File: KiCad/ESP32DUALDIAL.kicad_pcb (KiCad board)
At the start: 2 copper layers, 200 x 70 mm, 39 parts, among them J1 SERVICE, J2 100V IN, J3 FAN, J4 FAN, J5 POWER CONTROL, Q1 Q_NMOS_GDS, SW1 Rotary_Encoder_Switch, SW2 Rotary_Encoder_Switch, U1 CR2013-MI2120, U2 ESP-WROOM-32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

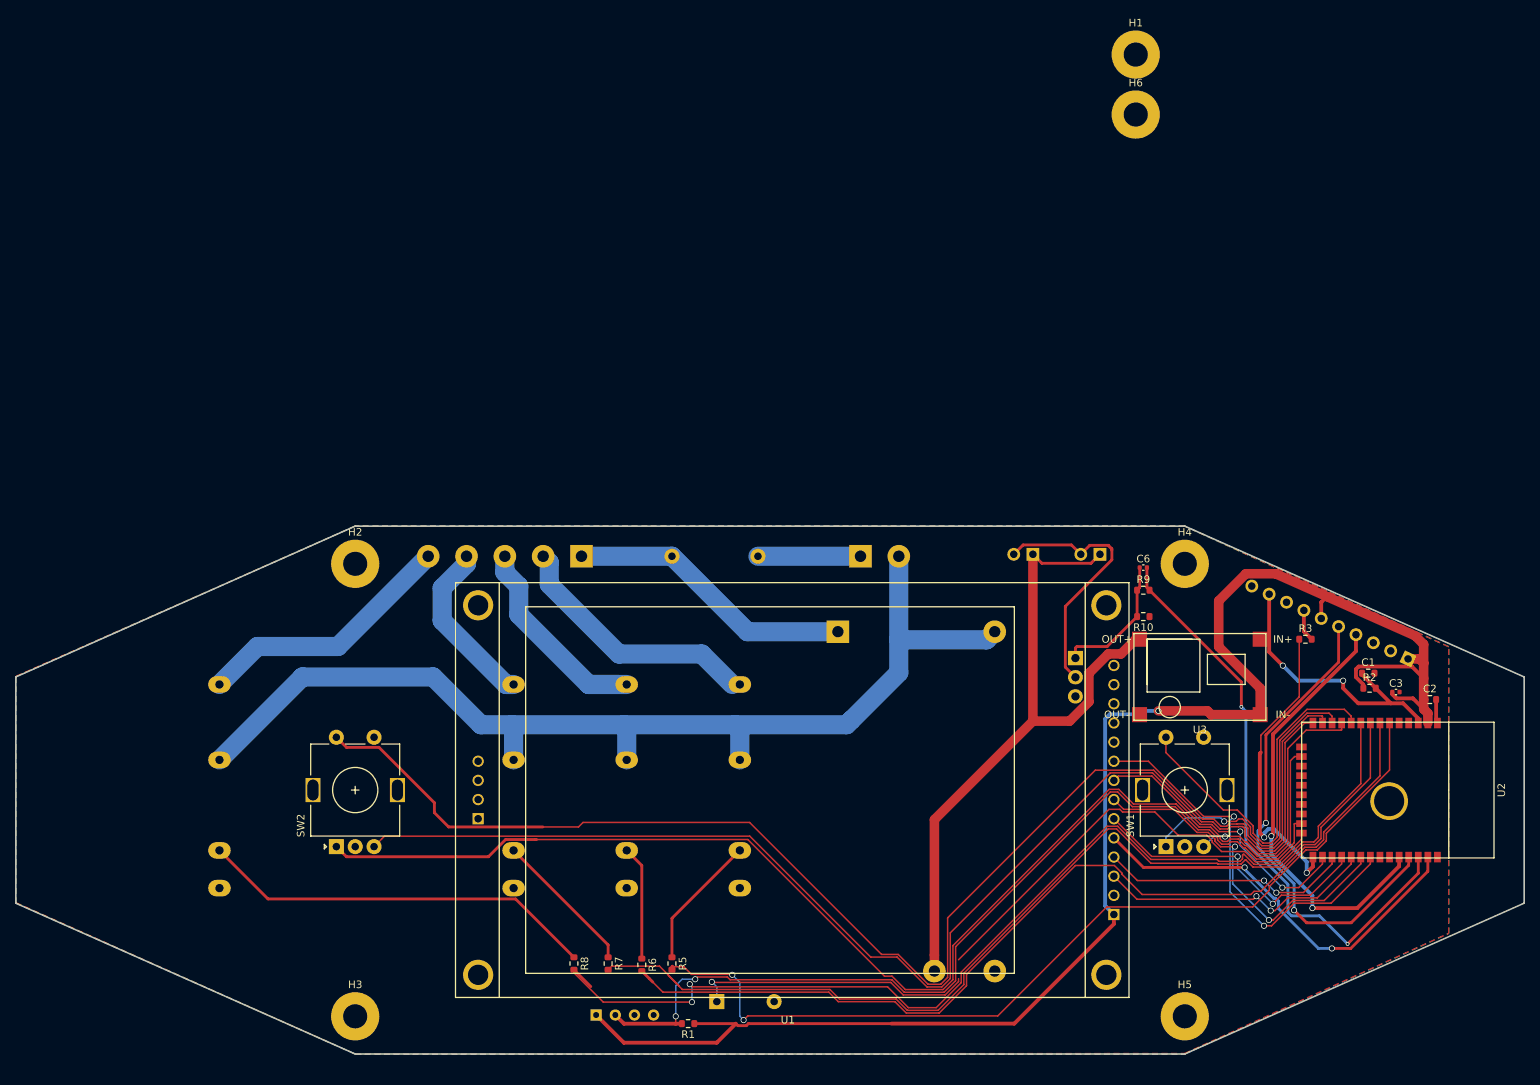
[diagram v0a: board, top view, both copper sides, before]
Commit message: change SSR SHARP S108T02
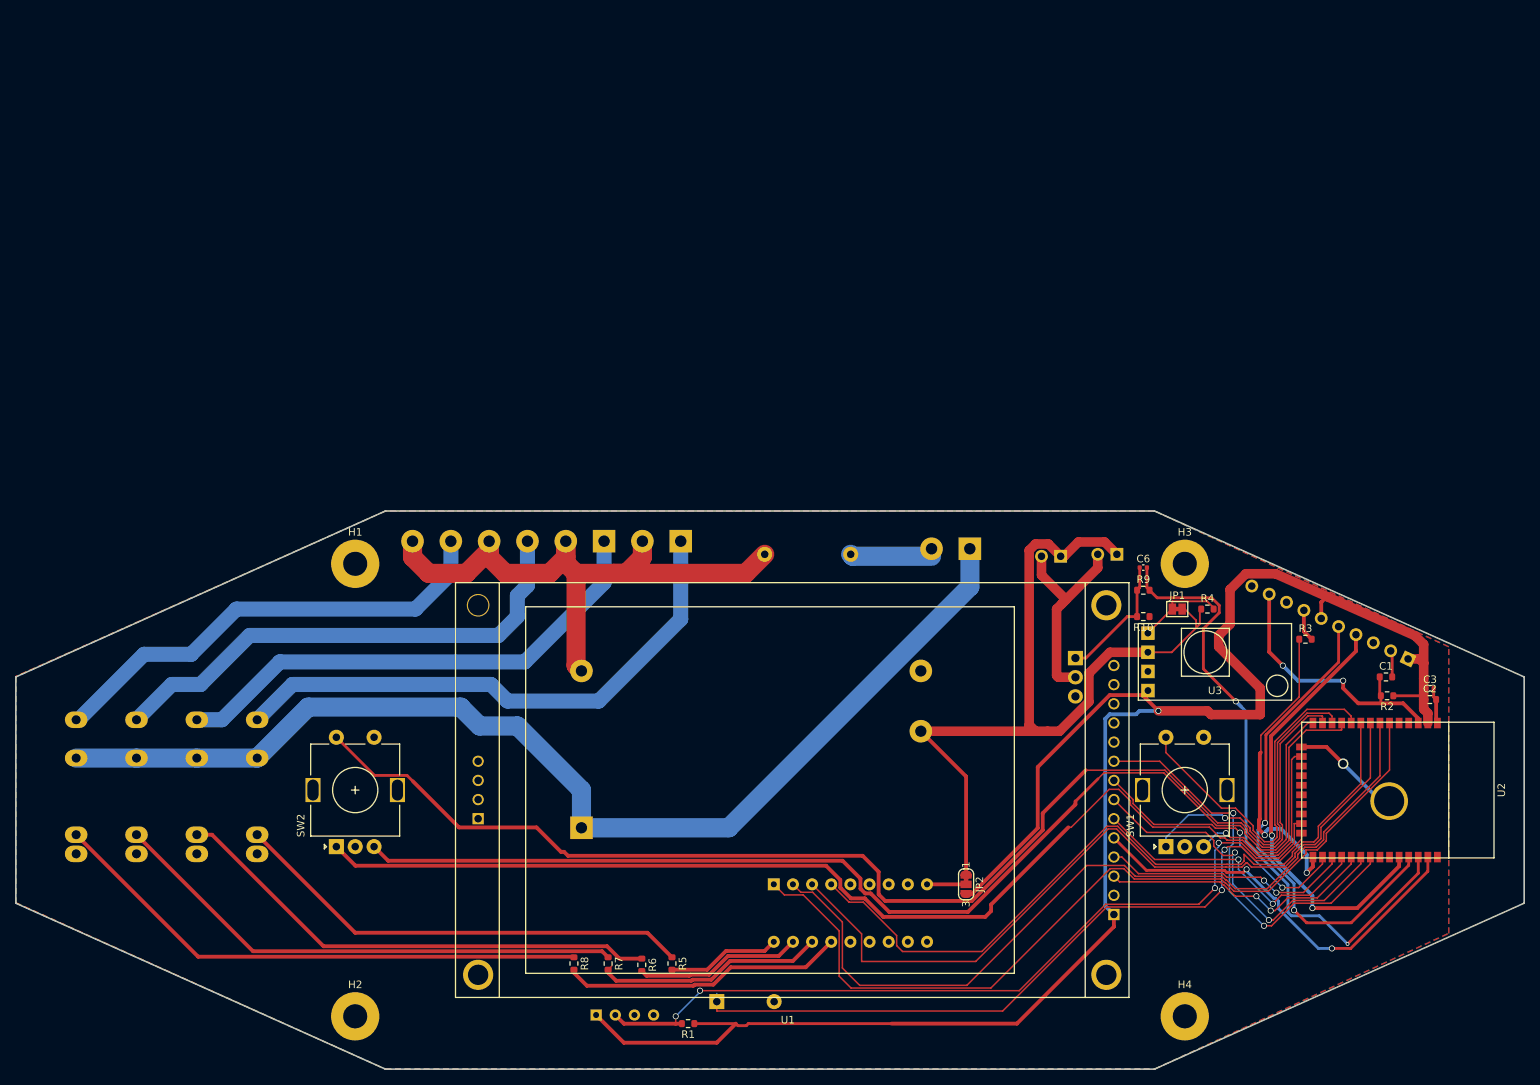
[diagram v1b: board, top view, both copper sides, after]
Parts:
- removed H5, H6: MountingHole_Pad, MountingHole:MountingHole_3.2mm_M3_Pad
- added J6: Conn_01x06_Male, TerminalBlock:TerminalBlock_bornier-6_P5.08mm, B.Cu at (93.0, 77.0)
- added JP1: Jumper, Jumper:SolderJumper-2_P1.3mm_Bridged_Pad1.0x1.5mm, F.Cu at (169.0, 86.0)
- added JP2: Jumper_NC_Dual, Jumper:SolderJumper-3_P1.3mm_Bridged12_RoundedPad1.0x1.5mm_NumberLabels, F.Cu at (141.0, 122.5)
- added R4: NC, Resistor_SMD:R_0603_1608Metric, F.Cu at (173.0, 86.0)
- added U9: TBD62783A, Package_DIP:DIP-18_W7.62mm, B.Cu at (115.5, 122.5)
- J5: value POWER CONTROL -> Conn_01x02_Male; footprint TerminalBlock:TerminalBlock_bornier-5_P5.08mm -> TerminalBlock:TerminalBlock_bornier-2_P5.08mm
- R5, R6, R7, R8: value 220 -> 330
- U3: value Mini-360 -> QS-1205CME-3A_MINIDC-DC_12-24Vto5V3A_1.8V_2.5V_3.3V_5V_9V_12V; footprint library:Mini-360_DCDC_LM2596_module -> library:QS-1205CME-3A_MINIDC-DC_12-24Vto5V3A_1.8V_2.5V_3.3V_5V_9V_12V
- U5, U6, U7, U8: value S112S01 -> S108T02; footprint library:SSR_NNC_NNG1D -> library:SSR_SHARP_S108T02
- moved H3 125.3 mm to (170.0, 80.0)
- moved H1 123.6 mm to (60.0, 80.0)
- moved U5 64.0 mm to (47.0, 109.6)
- moved H2 60.0 mm to (60.0, 140.0)
- moved H4 60.0 mm to (170.0, 140.0)
- moved U6 57.0 mm to (39.0, 109.6)
- moved U7 50.0 mm to (31.0, 109.6)
- moved PS1 42.8 mm to (90.0, 115.0), turned to 0 degrees
- moved U8 19.0 mm to (23.0, 109.6)
- moved J2 14.5 mm to (141.5, 78.0), turned to 180 degrees
- moved J5 13.3 mm to (103.2, 77.0)
- moved F1 12.3 mm to (114.3, 78.7)
- moved C3 4.55 mm to (202.5, 96.5)
- moved J3 3.69 mm to (153.5, 79.0)
- moved U3 2.83 mm to (174.0, 93.0), turned to 180 degrees
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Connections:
- J2 pad 1: Net-(F1-Pad2) -> Net-(J2-Pad1)
- J2 pad 2: Net-(J2-Pad2) -> Net-(F1-Pad2)
- J5 pad 1: Net-(F1-Pad1) -> Net-(J5-Pad1)
- J5 pad 2: Net-(J5-Pad2) -> Net-(F1-Pad1)
- PS1 pad 1: Net-(F1-Pad1) -> Net-(J2-Pad1)
- PS1 pad 2: Net-(J2-Pad2) -> Net-(F1-Pad1)
- R5 pad 2: PUMP -> Net-(R5-Pad2)
- R6 pad 2: OZON0 -> Net-(R6-Pad2)
- R7 pad 2: OZON1 -> Net-(R7-Pad2)
- R8 pad 2: OZON2 -> Net-(R8-Pad2)
- U3 pad 1: GND -> +3V3
- U3 pad 2: +3V3 -> GND
- U5 pad 1: Net-(J5-Pad2) -> Net-(J5-Pad1)
- U5 pad 2: Net-(J2-Pad2) -> Net-(J2-Pad1)
- U6 pad 1: Net-(J5-Pad3) -> Net-(J6-Pad1)
- U6 pad 2: Net-(J2-Pad2) -> Net-(J2-Pad1)
- U7 pad 1: Net-(J5-Pad4) -> Net-(J6-Pad3)
- U7 pad 2: Net-(J2-Pad2) -> Net-(J2-Pad1)
- U8 pad 1: Net-(J5-Pad5) -> Net-(J6-Pad5)
- U8 pad 2: Net-(J2-Pad2) -> Net-(J2-Pad1)
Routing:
- net Net-(J2-Pad1): track 0.00 -> 149.0 mm
- net Net-(J2-Pad2): track 143.2 -> 0.00 mm
- net Net-(J5-Pad1): track 0.00 -> 73.8 mm
- net Net-(J6-Pad1): track 0.00 -> 67.0 mm
- net Net-(J6-Pad3): track 0.00 -> 66.7 mm
- net Net-(J6-Pad5): track 0.00 -> 62.0 mm
- net Net-(R6-Pad1): track 15.2 -> 65.8 mm
- net Net-(R7-Pad1): track 19.4 -> 69.3 mm
- net Net-(F1-Pad1): track 38.1 -> 82.8 mm
- net Net-(R5-Pad1): track 17.9 -> 61.7 mm
- net OZON2: track 140.9 -> 98.9 mm, vias 2 -> 0
- net Net-(R8-Pad2): track 0.00 -> 37.6 mm
- net Net-(J5-Pad5): track 34.7 -> 0.00 mm
- net Net-(J5-Pad2): track 33.8 -> 0.00 mm
- net Net-(R7-Pad2): track 0.00 -> 30.7 mm
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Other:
- board size 200 x 70 mm -> 200 x 74 mm

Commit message: version 20210119
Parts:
- added C10: 10u, Capacitor_SMD:C_0402_1005Metric, F.Cu at (156.4, 113.8)
- added C11: 10u, Capacitor_SMD:C_0402_1005Metric, F.Cu at (147.6, 131.8)
- added C12: 0.1uF, Resistor_SMD:R_0603_1608Metric, F.Cu at (70.2, 99.8)
- added C4: 0.1uF, Resistor_SMD:R_0603_1608Metric, F.Cu at (164.8, 121.6)
- added C5: 0.1uF, Resistor_SMD:R_0603_1608Metric, F.Cu at (70.2, 105.5)
- added C7: 0.1uF, Resistor_SMD:R_0603_1608Metric, F.Cu at (70.2, 102.4)
- added C8: 0.1uF, Resistor_SMD:R_0603_1608Metric, F.Cu at (163.6, 117.8)
- added C9: 0.1uF, Resistor_SMD:R_0603_1608Metric, F.Cu at (164.0, 119.6)
- added D1: D_Schottky, Diode_SMD:D_SOD-123F, F.Cu at (151.0, 134.4)
- added J7: Conn_01x02_Male, Connector_JST:JST_NV_B02P-NV_1x02_P5.00mm_Vertical, B.Cu at (39.0, 127.5)
- added J8: Conn_01x02_Male, Connector_JST:JST_NV_B02P-NV_1x02_P5.00mm_Vertical, B.Cu at (29.0, 123.0)
- F1: footprint Fuse:Fuse_Littelfuse-LVR200 -> library:20mmFuse_P5x2
- J2: value 100V IN -> Conn_01x04_Male; footprint TerminalBlock:TerminalBlock_bornier-2_P5.08mm -> Connector_JST:JST_NV_B04P-NV_1x04_P5.00mm_Vertical
- J5: value Conn_01x02_Male -> Conn_01x03_Male; footprint TerminalBlock:TerminalBlock_bornier-2_P5.08mm -> Connector_JST:JST_VH_B3P-VH_1x03_P3.96mm_Vertical
- J6: value Conn_01x06_Male -> Conn_01x02_Male; footprint TerminalBlock:TerminalBlock_bornier-6_P5.08mm -> Connector_JST:JST_NV_B02P-NV_1x02_P5.00mm_Vertical
- moved J2 72.1 mm to (103.0, 139.0), turned to 0 degrees
- moved J6 70.4 mm to (49.0, 132.0), turned to 335 degrees
- moved J3 64.7 mm to (144.0, 143.0)
- moved J4 64.5 mm to (155.0, 143.0)
- moved J5 64.1 mm to (87.0, 139.0), turned to 0 degrees
- moved R1 60.0 mm to (105.2, 81.0)
- moved U4 58.8 mm to (92.0, 81.0)
- moved BZ1 52.5 mm to (115.0, 86.0), turned to 90 degrees
- moved F1 52.2 mm to (97.0, 128.0)
- moved U9 49.5 mm to (149.0, 86.0), turned to 90 degrees
- moved R6 46.0 mm to (99.0, 87.2)
- moved R8 45.9 mm to (91.0, 87.2)
- moved R7 45.8 mm to (95.0, 87.2)
- moved R5 45.8 mm to (102.0, 87.2)
- moved C6 36.2 mm to (156.3, 115.8)
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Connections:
- J5 pad 2: Net-(F1-Pad1) -> Net-(J5-Pad2)
- J6 pad 2: Net-(F1-Pad1) -> Net-(J2-Pad1)
- PS1 pad 1: Net-(J2-Pad1) -> Net-(F1-Pad1)
- PS1 pad 2: Net-(F1-Pad1) -> Net-(J2-Pad1)
- U5 pad 2: Net-(J2-Pad1) -> Net-(F1-Pad1)
- U6 pad 2: Net-(J2-Pad1) -> Net-(F1-Pad1)
- U7 pad 1: Net-(J6-Pad3) -> Net-(J7-Pad1)
- U7 pad 2: Net-(J2-Pad1) -> Net-(F1-Pad1)
- U8 pad 1: Net-(J6-Pad5) -> Net-(J8-Pad1)
- U8 pad 2: Net-(J2-Pad1) -> Net-(F1-Pad1)
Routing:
- net GND: track 23.0 -> 97.0 mm, vias 1 -> 4
- net Net-(J6-Pad3): track 66.7 -> 0.00 mm
- net Net-(J6-Pad5): track 62.0 -> 0.00 mm
- net Net-(J6-Pad1): track 67.0 -> 14.6 mm
- net +3V3: track 242.7 -> 195.0 mm, vias 1 -> 3
- net FAN: track 84.5 -> 39.7 mm, vias 2 -> 0
- net PUMP: track 112.4 -> 69.2 mm
- net Net-(R5-Pad2): track 15.0 -> 55.0 mm
- net OZON0: track 108.9 -> 69.9 mm
- net Net-(R6-Pad2): track 22.2 -> 55.8 mm
- net OZON1: track 103.6 -> 71.4 mm
- net OZON2: track 98.9 -> 67.9 mm
- net Net-(J1-Pad5): track 64.2 -> 34.9 mm, vias 2 -> 3
- net Net-(R7-Pad2): track 30.7 -> 57.7 mm
- net Net-(J5-Pad1): track 73.8 -> 46.9 mm
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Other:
- board size 200 x 74 mm -> 180.5 x 74 mm
- board text added: "0.1uF x 2"
- board text added: "0.1uF x 3"
- board text added: "100k 1k-"
- board text added: "10k"
- board text added: "10uF"
- board text added: "10uF 20pF"
- board text added: "270-470 x 4"
- board text added: "3V3 GND KEY RXD TXD 3V3 PRG GND RST GND"
- board text added: "4.7-10k"
- board text added: "ANTENNA WINDOW"
- board text added: "G D S NMOS"
- board text removed: "3V3 GND KEY TXD RXD 3V3 PRG GND RST GND"
- board text removed: "ANTENNA AREA"
